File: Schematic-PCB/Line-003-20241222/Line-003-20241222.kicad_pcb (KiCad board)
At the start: 4 copper layers, 196 x 193.6 mm, 245 parts, among them J1 VIN, J2 Conn_MD, U47 LM393, U48 LM393, U49 LM393, U50 LM393, U51 LM393, U52 LM393, U53 LM393, U54 LM393, U55 LM393, U56 LM393, U57 LM393, U58 LM393, U59 LM393, U60 LM393, U61 LM393, U62 ATmega2560 Pro Board

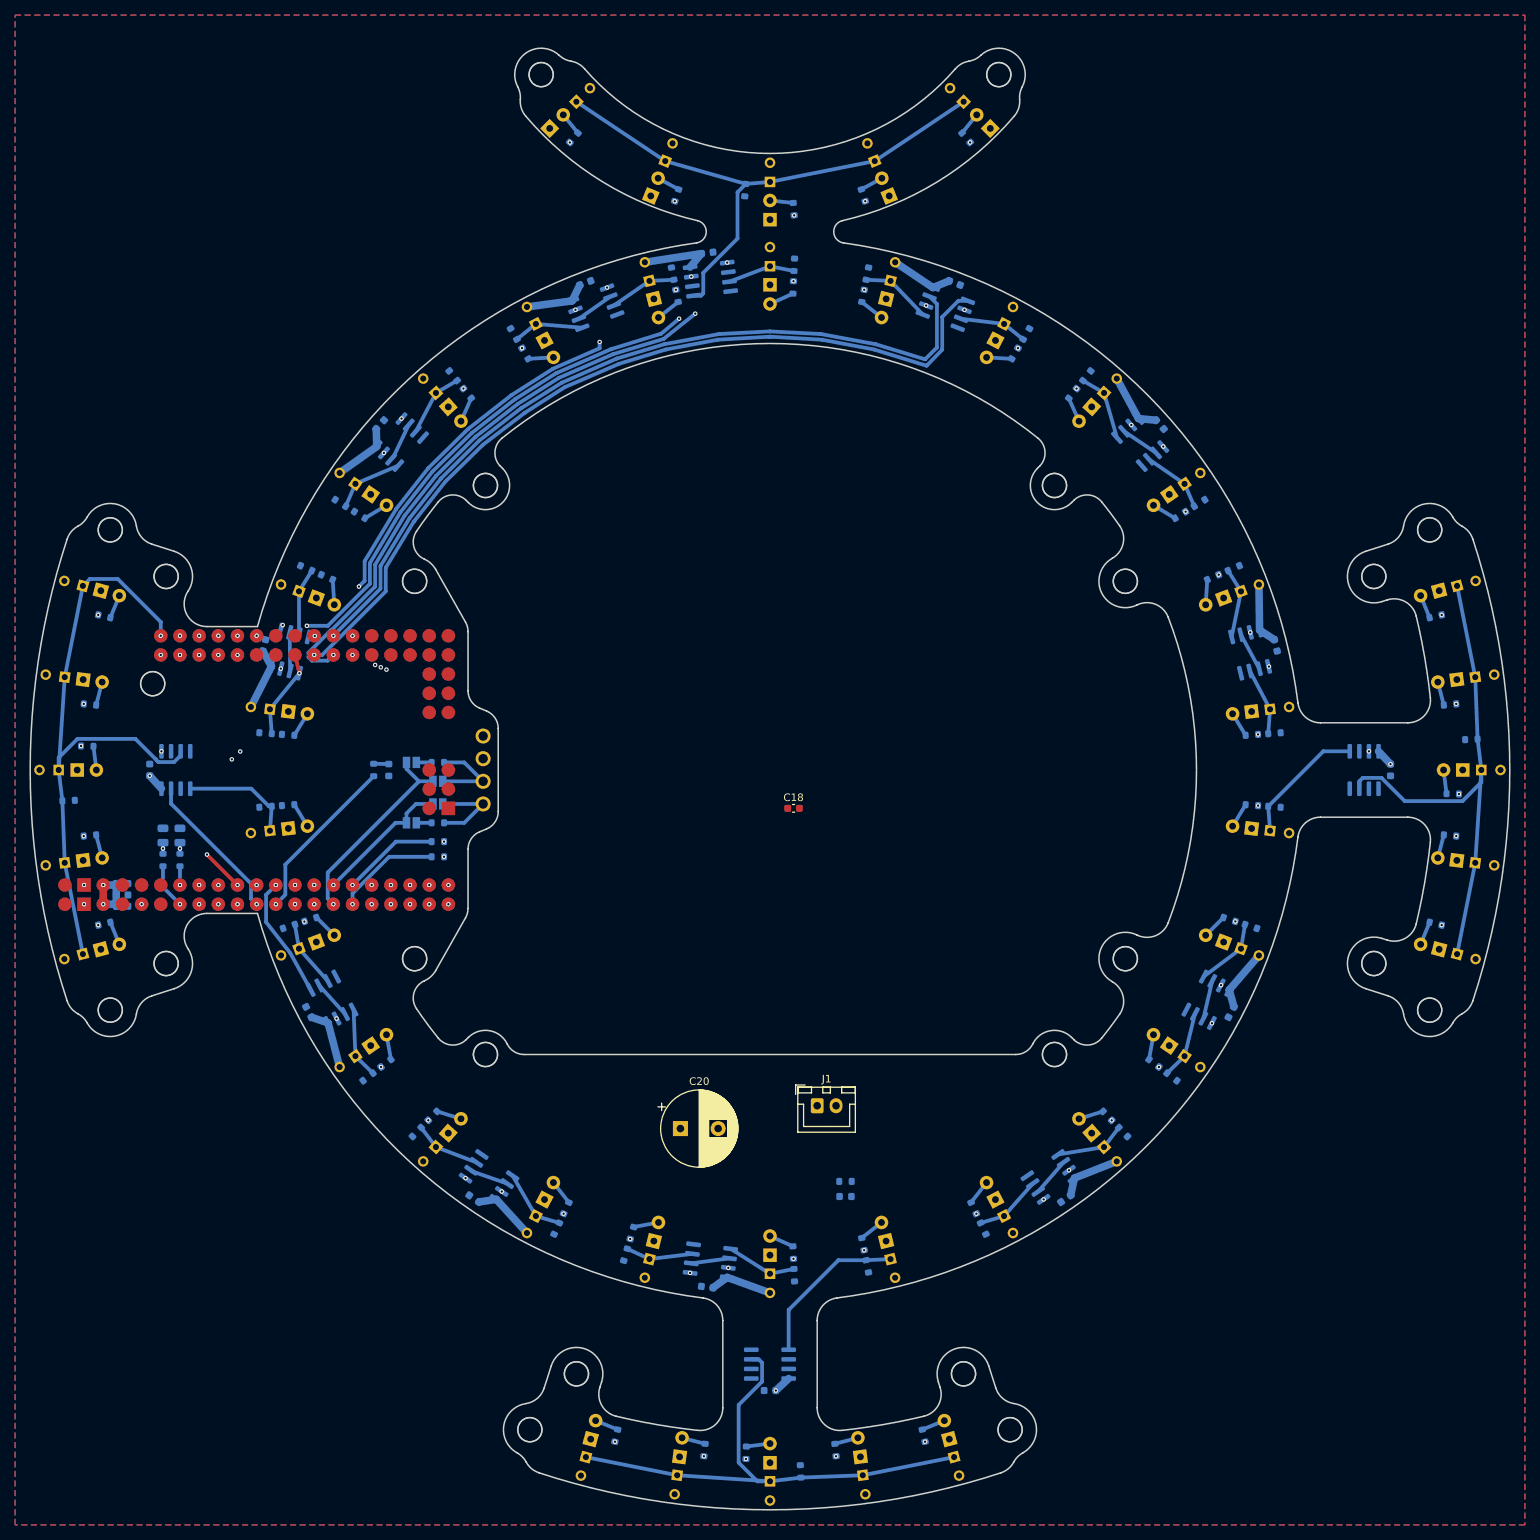
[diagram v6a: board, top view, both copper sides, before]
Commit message: update: ラインセンサ基板のPCBを更新した
配線を進めた
Thをベタ化して配線を楽にした
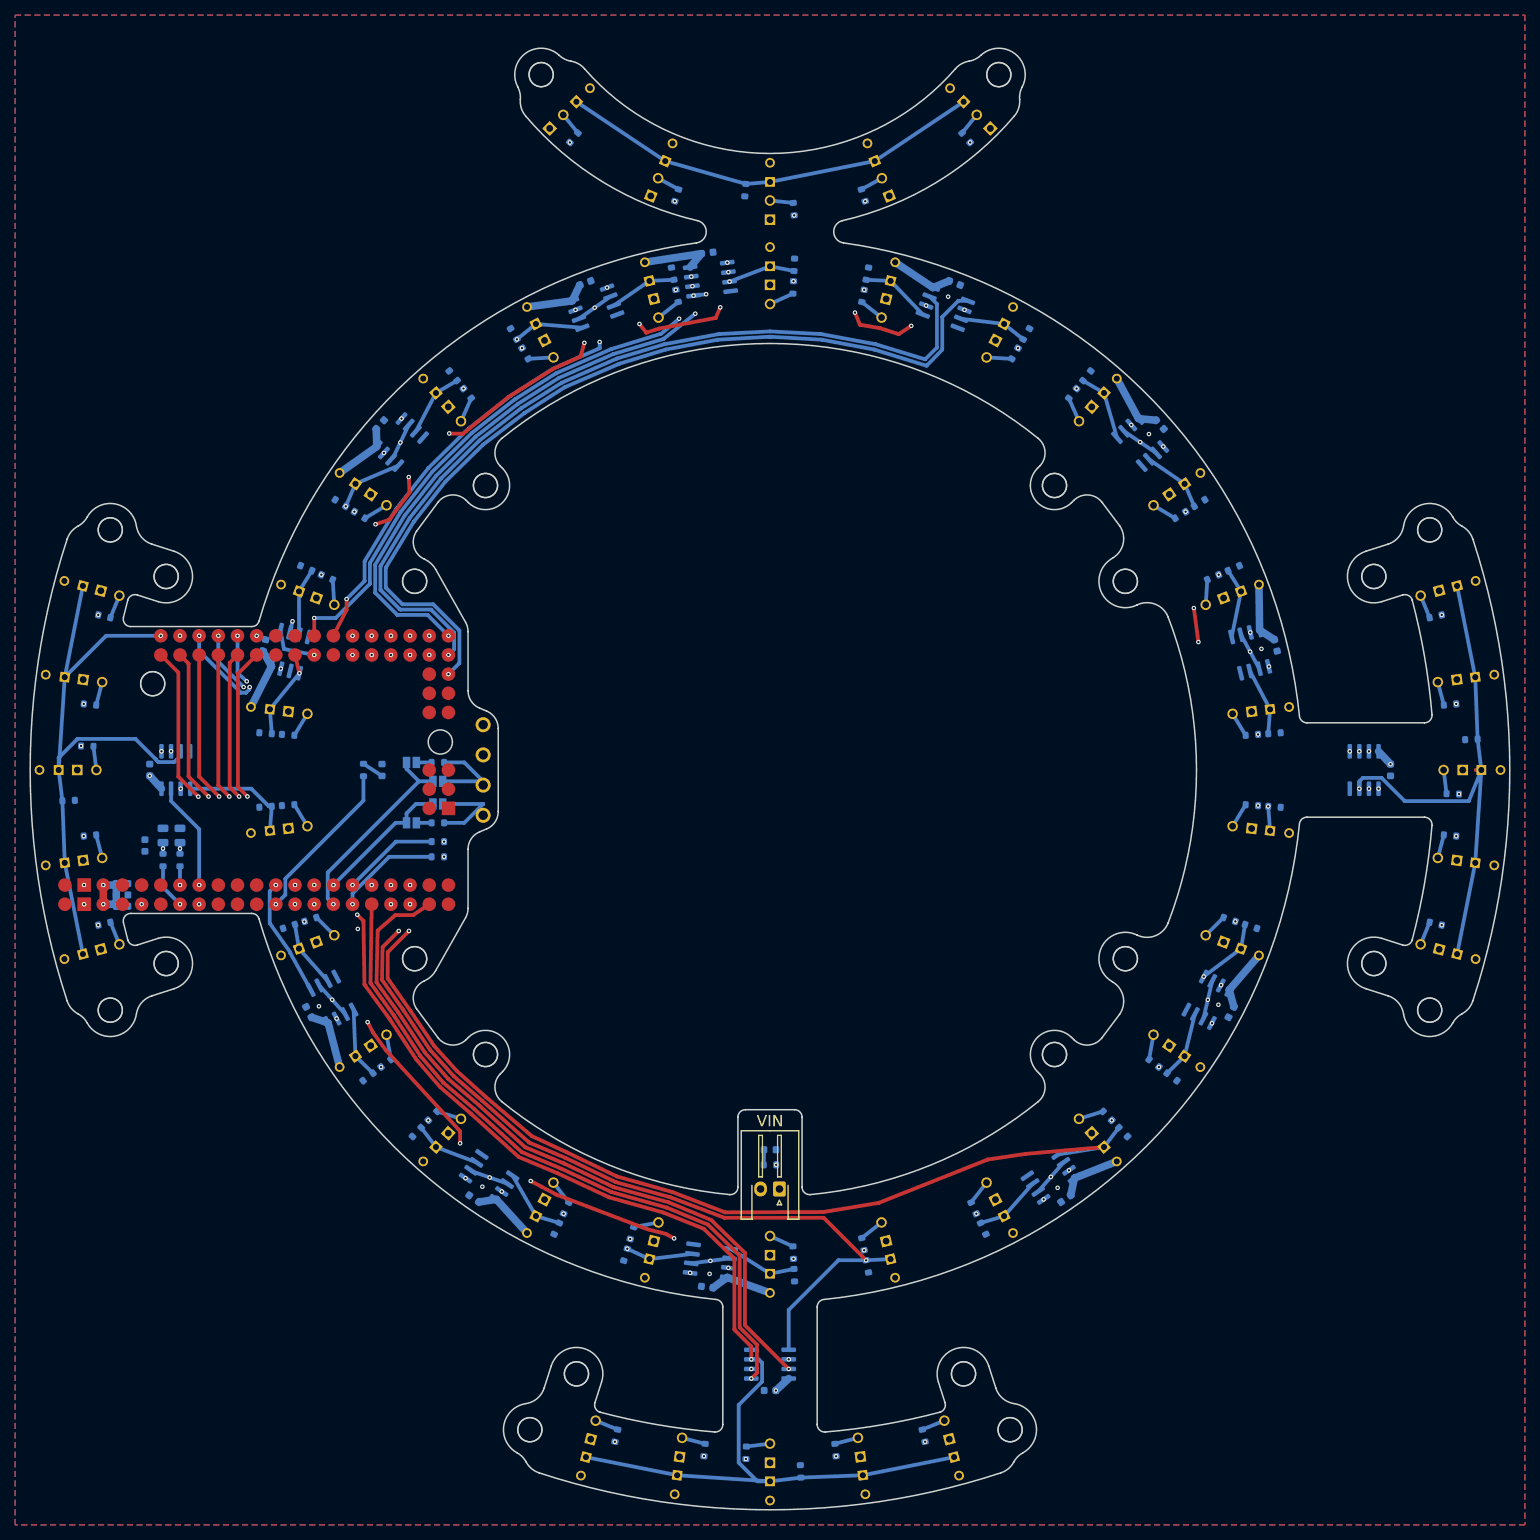
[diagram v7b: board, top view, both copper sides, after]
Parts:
- removed C20: 1000uF, Capacitor_THT:CP_Radial_D10.0mm_P5.00mm
- C18: moved to B.Cu
- J1: footprint Connector_JST:JST_XH_B2B-XH-A_1x02_P2.50mm_Vertical -> Connector_JST:JST_XH_S2B-XH-A-1_1x02_P2.50mm_Horizontal
- moved C18 86.1 mm to (-82.8, 10.0), turned to -90 degrees
- moved J1 12.1 mm to (1.25, 55.5), turned to 180 degrees
- moved D48 11.8 mm to (0.00, 50.3), turned to 180 degrees
- moved R88 10.2 mm to (0.00, 52.3), turned to 0 degrees
- moved R79 1.35 mm to (-53.9, 0.00)
- moved D47 0.90 mm to (-51.4, 0.00), turned to -90 degrees
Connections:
- C21 pad 1: Threshold -> Th
- C22 pad 1: Threshold2 -> Th2
- R81 pad 2: Threshold -> Th
- R84 pad 2: Threshold2 -> Th2
- U62 pad A1: Line03 -> Line09
- U62 pad A10: Line21 -> Line23
- U62 pad A11: Line23 -> Line17
- U62 pad A12: Line-F -> Line21
- U62 pad A13: Line01 -> Line19
- U62 pad A14: Line-B -> Line-R
- U62 pad A3: Line-R -> Line11
- U62 pad A4: Line09 -> Line03
- U62 pad A5: Line11 -> Line13
- U62 pad A6: Line13 -> Line01
- U62 pad A7: Line15 -> Line-B
- U62 pad A8: Line17 -> Line-F
- U62 pad A9: Line19 -> Line15
- U62 pad D10: 07 -> unconnected-(U62-PadD10)
- U62 pad D11: 08 -> unconnected-(U62-PadD11)
- U62 pad D23: 15 -> B
- U62 pad D28: 20 -> unconnected-(U62-PadD28)
- U62 pad D29: 21 -> 15
- U62 pad D30: 22 -> unconnected-(U62-PadD30)
- U62 pad D31: 23 -> unconnected-(U62-PadD31)
- U62 pad D32: 24 -> 01
- U62 pad D33: 25 -> 06
- U62 pad D34: 26 -> 02
- U62 pad D35: F -> unconnected-(U62-PadD35)
- U62 pad D36: L -> 05
- U62 pad D37: B -> 04
- U62 pad D38: R -> 03
- U62 pad D39: unconnected-(U62-PadD39) -> 07
- U62 pad D4: 01 -> 08
- U62 pad D40: unconnected-(U62-PadD40) -> R
- U62 pad D41: unconnected-(U62-PadD41) -> 24
- U62 pad D42: unconnected-(U62-PadD42) -> 20
- U62 pad D43: unconnected-(U62-PadD43) -> 23
- U62 pad D44: unconnected-(U62-PadD44) -> 22
- U62 pad D45: unconnected-(U62-PadD45) -> 21
- U62 pad D46: unconnected-(U62-PadD46) -> F
- U62 pad D47: unconnected-(U62-PadD47) -> 26
- U62 pad D48: unconnected-(U62-PadD48) -> 25
- U62 pad D5: 02 -> L
- U62 pad D6: 03 -> unconnected-(U62-PadD6)
- U62 pad D7: 04 -> unconnected-(U62-PadD7)
- U62 pad D8: 05 -> unconnected-(U62-PadD8)
- U62 pad D9: 06 -> unconnected-(U62-PadD9)
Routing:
- net R: track 0.00 -> 180.8 mm, vias 0 -> 2
- net Line17: track 9.40 -> 184.5 mm, vias 1 -> 2
- net Line15: track 21.5 -> 166.6 mm, vias 1 -> 3
- net Line-B: track 70.6 -> 204.0 mm, vias 0 -> 3
- net Line-F: track 75.0 -> 190.0 mm, vias 0 -> 4
- net Line01: track 8.97 -> 119.5 mm, vias 0 -> 3
- net Line13: track 8.97 -> 117.2 mm, vias 1 -> 3
- net Th: track 56.3 -> 152.1 mm, vias 2 -> 31
- net 15: track 0.00 -> 95.0 mm
- net B: track 0.00 -> 90.6 mm
- net Line11: track 8.97 -> 91.8 mm
- net Line03: track 9.40 -> 83.6 mm, vias 1 -> 3
- net 05: track 75.4 -> 26.6 mm, vias 4 -> 2
- net Line09: track 8.97 -> 57.1 mm
- net 02: track 109.9 -> 62.3 mm, vias 4 -> 3
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- added copper zone on In2.Cu, net Th
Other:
- outline, holes or cut-outs redrawn
- board text added: "VIN"
